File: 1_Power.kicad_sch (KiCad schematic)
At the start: 35 parts, among them Q201 IRLZ44N, Q202 IRLZ44N, U201 BQ24005, U202 LM74700, U203 LM74700, U204 TLV75733PDBV, U205 LMR51430, U206 TPS7A2033PDBVR

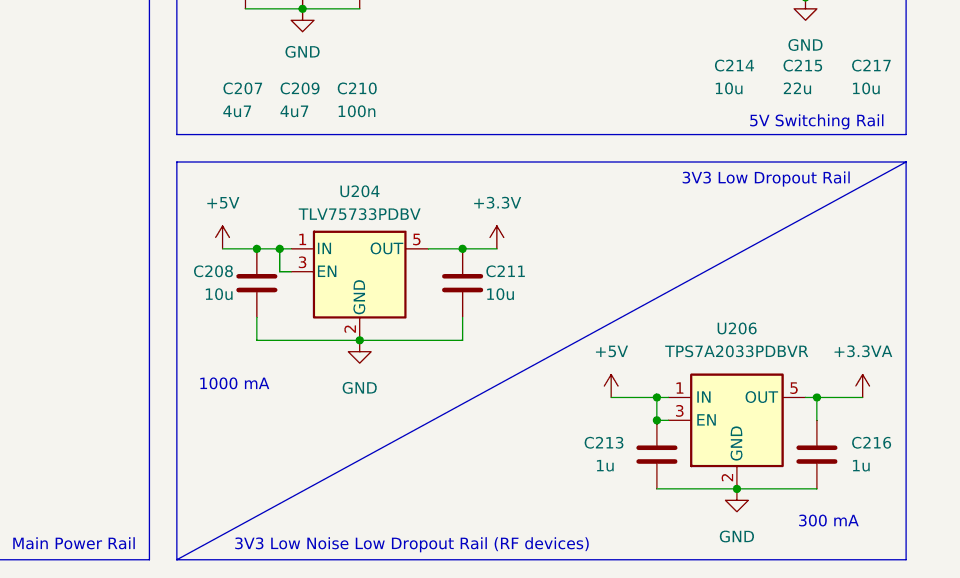
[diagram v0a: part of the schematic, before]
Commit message: Major changes
Updated schematic for better power delivery
Changed 3.3V supply to buck converter instead of LDO due to heat
Deleted the entire PCB, redoing the whole thing due to problems in
laying traces that made some connections impossible to make
Also updated README to reflect these changes
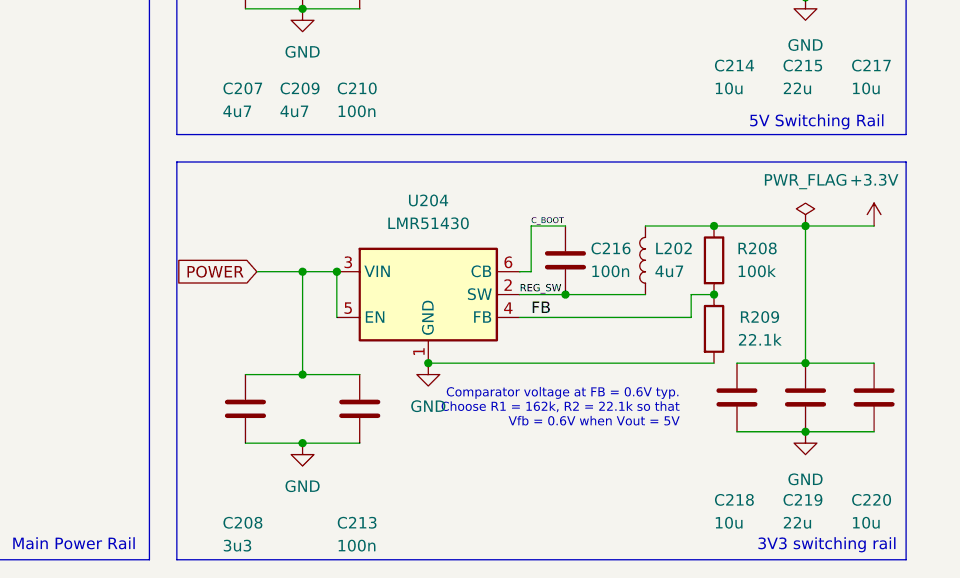
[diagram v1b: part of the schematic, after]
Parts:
- removed C211: 10u, Capacitor_SMD:C_0805_2012Metric, symbol Device:C
- removed U204: TLV75733PDBV, Package_TO_SOT_SMD:SOT-23-5, symbol Regulator_Linear:TLV75733PDBV
- removed U206: TPS7A2033PDBVR, Package_TO_SOT_SMD:SOT-23-5, symbol Regulator_Linear:TPS7A20xxxDBV
- added C218, C220: 10u, Capacitor_SMD:C_0805_2012Metric, symbol Device:C
- added C219: 22u, Capacitor_SMD:C_0805_2012Metric, symbol Device:C
- added L202: 4u7, Inductor_SMD:L_Sunlord_SWPA8040S, symbol Device:L
- added R208: 100k, Resistor_SMD:R_0603_1608Metric, symbol Device:R
- added R209: 22.1k, Resistor_SMD:R_0603_1608Metric, symbol Device:R
- added U204: LMR51430, Package_TO_SOT_SMD:SOT-23-6, symbol Regulator_Switching:LMR51430
- C208: value 10u -> 3u3; footprint Capacitor_SMD:C_0805_2012Metric -> Capacitor_SMD:C_0603_1608Metric
- C213, C216: value 1u -> 100n
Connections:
- net +3.3VA is gone; now on net C_BOOT: C216.1
- net +3.3V: now also C218.1, C219.1, C220.1, L202.2, R208.1
- net +5V: no longer C208.1, C213.1
- net C_BOOT: now also U204.6 (CB)
- net FB: now also R208.2, R209.1, U204.4 (FB)
- net GND: now also C218.2, C219.2, C220.2, R209.2, U204.1 (GND); no longer C216.2
- net POWER: now also C208.1, C213.1, U204.3 (VIN), U204.5 (EN)
- net REG_SW: now also C216.2, L202.1, U204.2 (SW)
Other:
- note added: "3V3 switching rail"
- note removed: "1000 mA"
- note removed: "300 mA"
- note removed: "3V3 Low Dropout Rail"
- note removed: "3V3 Low Noise Low Dropout Rail (RF devices)"

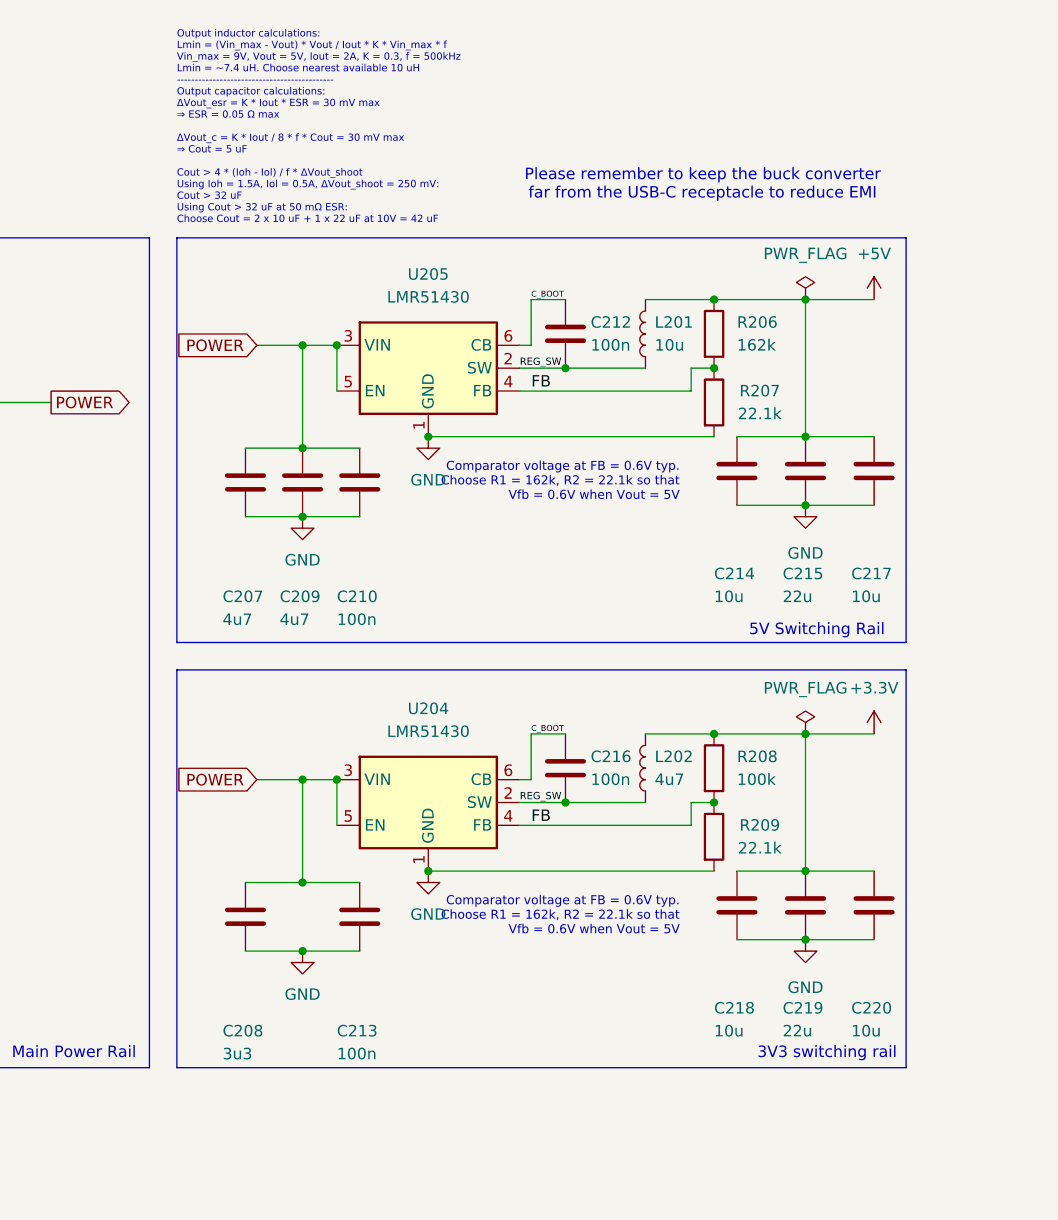
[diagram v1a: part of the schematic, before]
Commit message: Finished most of component re-placement
Began laying tracks for important connections
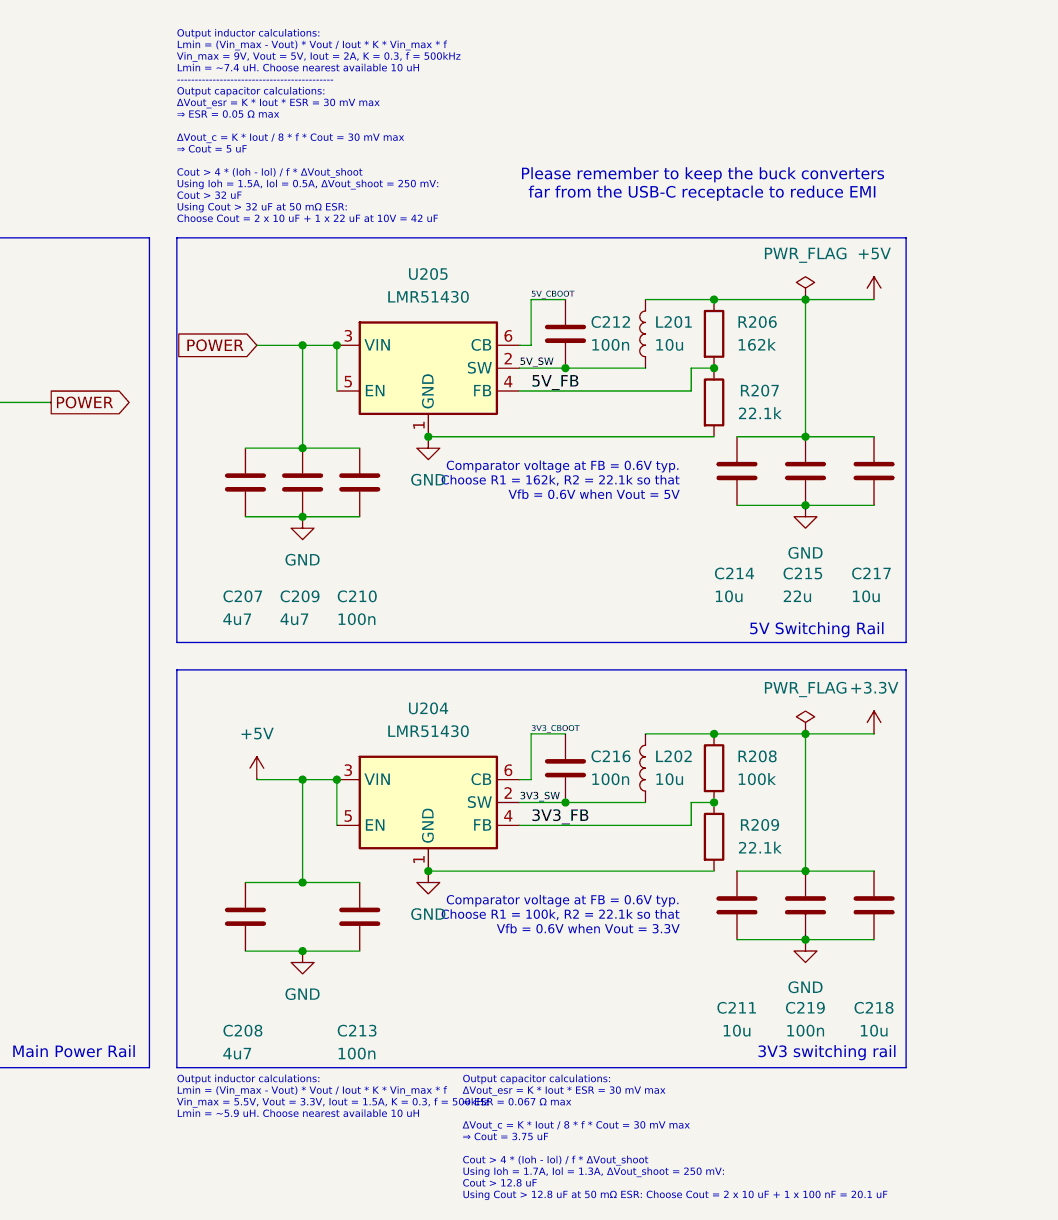
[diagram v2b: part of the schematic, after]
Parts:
- removed C220: 10u, Capacitor_SMD:C_0805_2012Metric, symbol Device:C
- added C211: 10u, Capacitor_SMD:C_0805_2012Metric, symbol Device:C
- C208: value 3u3 -> 4u7
- C219: value 22u -> 100n; footprint Capacitor_SMD:C_0805_2012Metric -> Capacitor_SMD:C_0603_1608Metric
- L202: value 4u7 -> 10u
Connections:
- net +3.3V: now also C211.1
- net +5V: now also C208.1, C213.1, U204.3 (VIN), U204.5 (EN)
- net GND: now also C211.2
- net POWER: no longer C208.1, C213.1, U204.3 (VIN), U204.5 (EN)
- net C_BOOT renamed 3V3_CBOOT
- net 3V3_CBOOT: no longer C212.1, U205.6 (CB)
- net FB renamed 3V3_FB
- net 3V3_FB: no longer R206.2, R207.1, U205.4 (FB)
- net REG_SW renamed 3V3_SW
- net 3V3_SW: no longer C212.2, L201.1, U205.2 (SW)
- new net 5V_CBOOT: C212.1, U205.6 (CB)
- new net 5V_FB: R206.2, R207.1, U205.4 (FB)
- new net 5V_SW: C212.2, L201.1, U205.2 (SW)
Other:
- note added: "Comparator voltage at FB = 0.6V typ. Choose R1 = 100k, R2 = 22.1k so that Vfb = 0.6V when Vout = 3.3V"
- note added: "Output capacitor calculations: ΔVout_esr = K * Iout * ESR = 30 mV max ⇒ ESR = 0.067 Ω max ΔVout_c = K * Iout / 8 * f * Cout = 30 mV max ⇒ Cout = 3.75 uF Cout > 4 * (Ioh - Iol) / f * ΔVout_shoot Using Ioh = 1.7A, Iol = 1.3A, ΔVout_shoot = 250 mV: Cout > 12.8 uF Using Cout > 12.8 uF at 50 mΩ ESR: Choose Cout = 2 x 10 uF + 1 x 100 nF = 20.1 uF"
- note added: "Output inductor calculations: Lmin = (Vin_max - Vout) * Vout / Iout * K * Vin_max * f Vin_max = 5.5V, Vout = 3.3V, Iout = 1.5A, K = 0.3, f = 500kHz Lmin = ~5.9 uH. Choose nearest available 10 uH"
- note added: "Please remember to keep the buck converters far from the USB-C receptacle to reduce EMI"
- note removed: "Please remember to keep the buck converter far from the USB-C receptacle to reduce EMI"

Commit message: Added more power (3.3V) headers for more powering peripherals
Continued laying out tracks
Revised order of connections to pyrochannel mux for easier routing
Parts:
- C207, C208, C209: value 4u7 -> 10u; footprint Capacitor_SMD:C_0603_1608Metric -> Capacitor_SMD:C_0805_2012Metric
- C215: value 22u -> 100n; footprint Capacitor_SMD:C_0805_2012Metric -> Capacitor_SMD:C_0603_1608Metric
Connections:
- net BATT_APG: no longer C201.1, U201.12 (CR)
- net GND: no longer C202.2
- net at C202.1: now also C201.1, U201.12 (CR); no longer U201.13 (TMR_SEL)
- new net: C202.2, U201.13 (TMR_SEL)
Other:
- moved on the sheet: C201, C202

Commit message: Revised schematic for easier routing
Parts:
- C205, C206: footprint Capacitor_SMD:C_0603_1608Metric -> Capacitor_SMD:C_0805_2012Metric
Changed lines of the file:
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@@
 			)
 		)
-		(property "Footprint" "Capacitor_SMD:C_0603_1608Metric"
+		(property "Footprint" "Capacitor_SMD:C_0805_2012Metric"
 			(at 162.2552 118.11 0)
 			(hide yes)
@@
 			)
 		)
-		(property "Footprint" "Capacitor_SMD:C_0603_1608Metric"
+		(property "Footprint" "Capacitor_SMD:C_0805_2012Metric"
 			(at 159.7152 74.93 0)
 			(hide yes)
